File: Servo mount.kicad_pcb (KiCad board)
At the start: 2 copper layers, 80 x 35.2 mm, 32 parts, among them CON1 2PIN_SCREWTERMINAL, CON2 2PIN_SCREWTERMINAL, IC1 ATTINY84-SS, K5 CONN_3, K6 CONN_3, M2 VAL**, P1 CONN_3X2, P2 CONN_2, Q1 BC847, Q2 BC847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

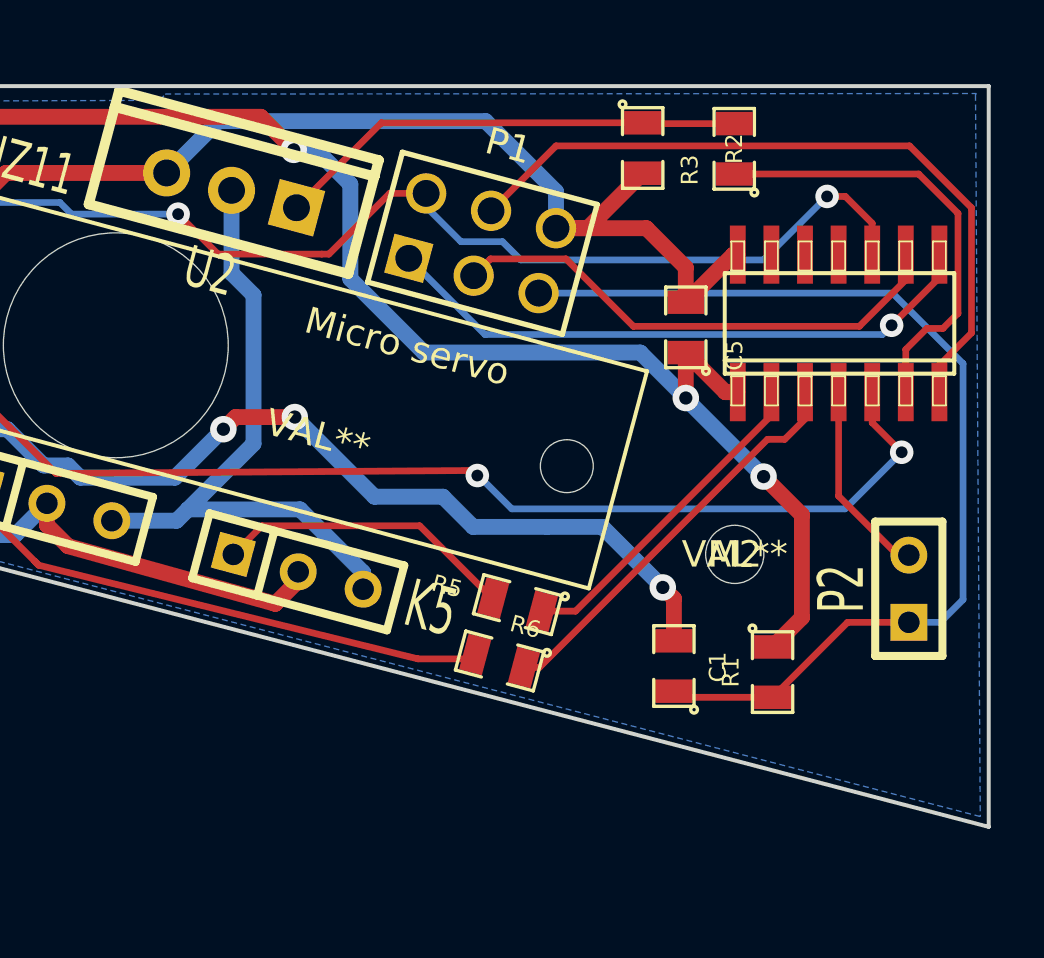
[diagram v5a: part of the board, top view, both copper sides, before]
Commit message: Solderpads for I/O (closes #1), reset solder jumper
Added solder pads for remaining I/O pins on the microcontroller, closes
#1
Change the reset jumper to a normally connected solder jumper with
through hole for debug wire.
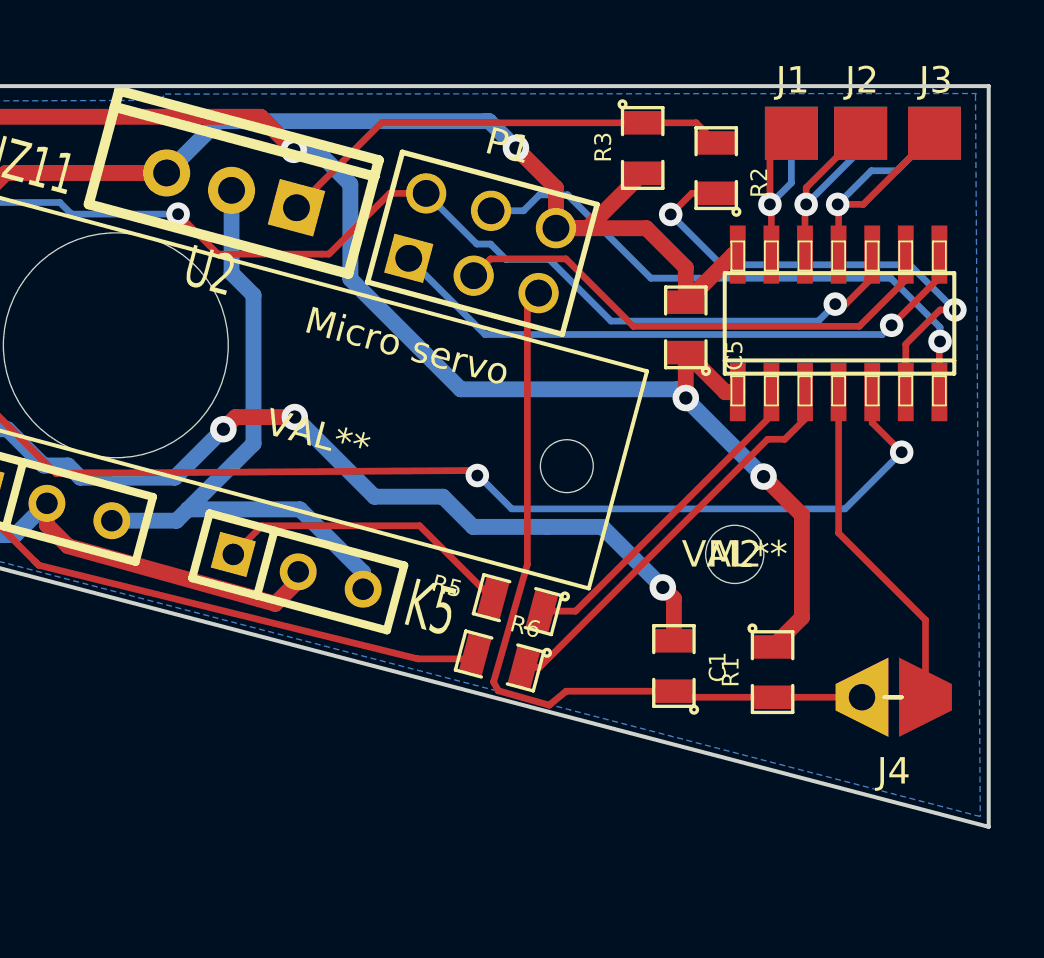
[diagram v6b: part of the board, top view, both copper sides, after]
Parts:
- removed P2: CONN_2, SIL-2
- added J1: ~, solder_pad_2mm_fb, F.Cu at (172.5, 101.8)
- added J2: ~, solder_pad_2mm_fb, F.Cu at (175.2, 101.8)
- added J3: ~, solder_pad_2mm_fb, F.Cu at (177.9, 101.8)
- added J4: ~, solder_jumper_conn, F.Cu at (176.4, 123.1)
- moved R2 1.00 mm to (169.7, 103.1)
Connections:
- IC1 pad 11: (no net) -> N-0000017
- IC1 pad 12: (no net) -> N-0000018
- IC1 pad 13: (no net) -> N-0000019
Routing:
- net N-0000017: track 0.00 -> 11.5 mm, vias 0 -> 1
- net Reset: track 38.6 -> 29.5 mm
- net N-0000018: track 0.00 -> 9.01 mm, vias 0 -> 1
- net N-0000019: track 0.00 -> 7.98 mm, vias 0 -> 1
- net MOSI: track 27.6 -> 21.8 mm, vias 0 -> 1
- net N-000009: track 7.51 -> 12.9 mm
- net GND FET: track 17.0 -> 18.5 mm, vias 0 -> 2
- net GND: track 167.3 -> 167.4 mm, vias 6 -> 7

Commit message: Fixed servo connection pins (closes #8) and servo connector holes (closes #6)
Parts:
- J1, J2, J3: value ~ -> SOLDER_PAD
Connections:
- IC1 pad 2: PB3 -> (no net)
- IC1 pad 3: PB4 -> (no net)
- R5 pad 1: PB3 -> MOSI
- R6 pad 1: PB4 -> MISO
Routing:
- net MOSI: track 21.8 -> 41.4 mm, vias 1 -> 2
- net MISO: track 23.0 -> 42.2 mm, vias 1 -> 2
- net PB4: track 15.5 -> 0.00 mm
- net PB3: track 12.6 -> 0.00 mm
- net +5V: vias 3 -> 2
